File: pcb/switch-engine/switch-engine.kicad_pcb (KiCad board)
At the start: 10 copper layers, 135 x 111 mm, 369 parts, among them J1 CONN_PCIE_PWR_8PIN, J10 CORTEX_DEBUG_ETM, J11 SMPM, J12 CONN_01X03, J13 PMOD_HOST, J14 ARF6-08-S-D-A-K-TR, J15 ARF6-08-S-D-A-K-TR, J16 CONN_01X10, J17 ARF6-08-S-D-A-K-TR, J18 ARF6-08-S-D-A-K-TR, J19 CONN_01X10, J2 CONN_IBC_MGMT, J20 0826-1G1T-23-F, J21 ARF6-08-S-D-A-K-TR, J22 ARF6-08-S-D-A-K-TR, J23 CONN_01X10, J24 SMPM, J26 RJ45, J3 CONN_01X03, J4 CORTEX_DEBUG_ETM, J5 FAN_01, J6 FAN_01, J7 JUMPER_0402, J8 XILINX_JTAG, J9 PMOD_HOST, M1 SCREWHOLE, M2 SCREWHOLE, M3 SCREWHOLE, M4 SCREWHOLE, M5 LOGO, M6 LOGO, M7 LOGO, M8 960-27-23-D-AB-0, M9 FAN, Q2 SSM6N58NU, SW1 SWITCH, SW2 SWITCH, U1 STM32L431-QFN48, U10 74LVC1T45, U11 74LVC1T45, U12 74LVC1T45, U13 MT25QU256ABA8E12-0AUT, U14 ECS-1612MV-250-CN, U15 SIT9121AI-2BF-XXS156.250000G, U17 AT24MAC402, U18 74LVC1T45, U19 74LVC1T45, U2 MYMGK1R812ERSR, U20 74LVC1T45, U21 74LVC1T45, U22 ECS-1612MV-250-CN, U23 KSZ9031RN, U24 ESD224DQAR, U25 SIT9121AI-2BF-XXS156.250000G, U26 ESD224DQAR, U27 SIT9121AI-2BF-XXS156.250000G, U28 ADP1740ACPZ-2.5-R7, U29 ADM3101E_QFN, U3 MYMGK1R812ERSR, U4 MYMGK00506ERSR, U5 MYMGK00504ERSR, U6 MYMGK00504ERSR, U7 ADP1740ACPZ-1.8-R7, U8 XCKU5P-2FFVB676I, U9 STM32H735-UFBGA176-25

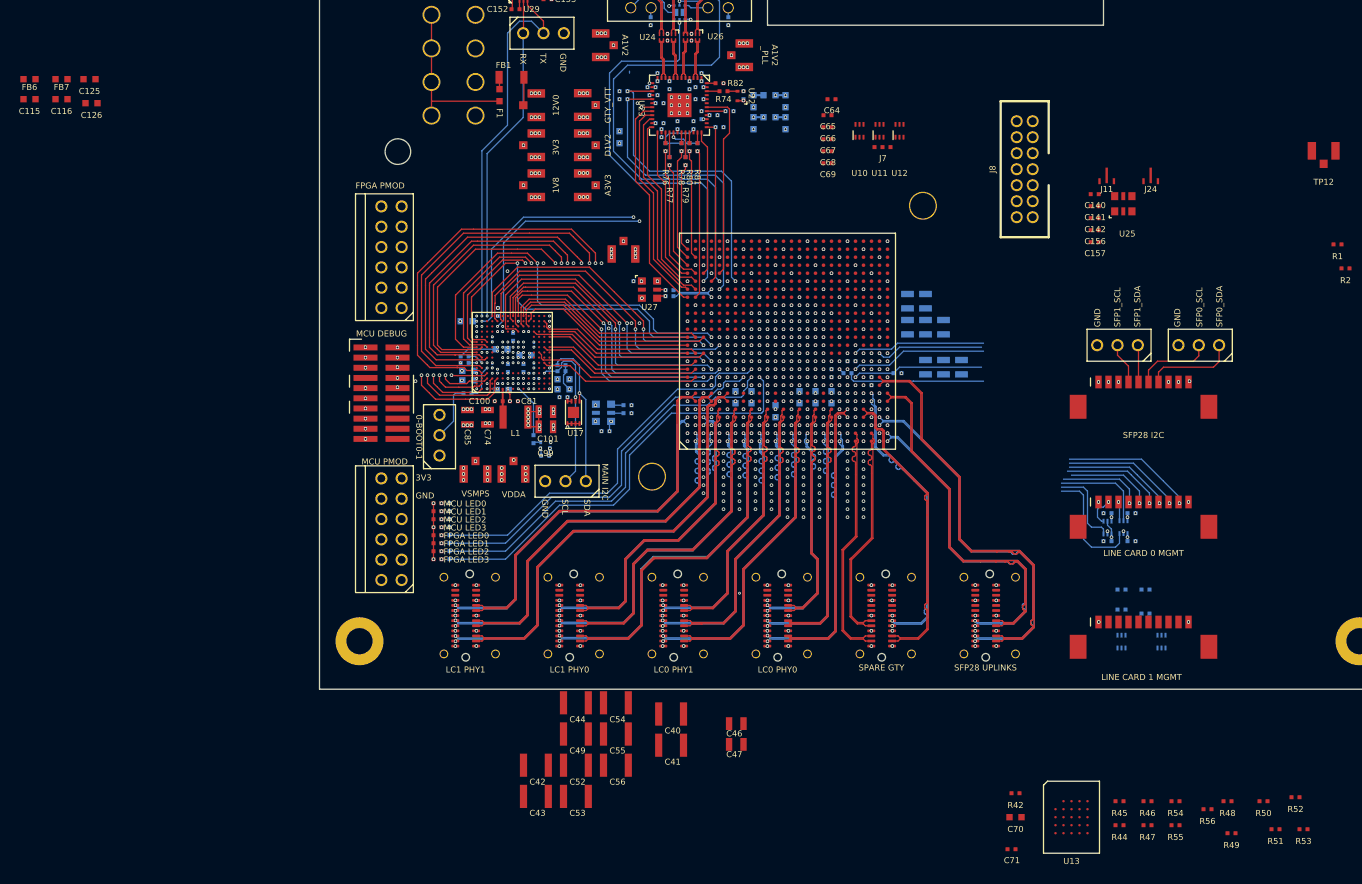
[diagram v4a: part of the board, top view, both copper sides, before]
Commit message: Continued routing main MCU and FPGA support parts, hooked up part of boot flash
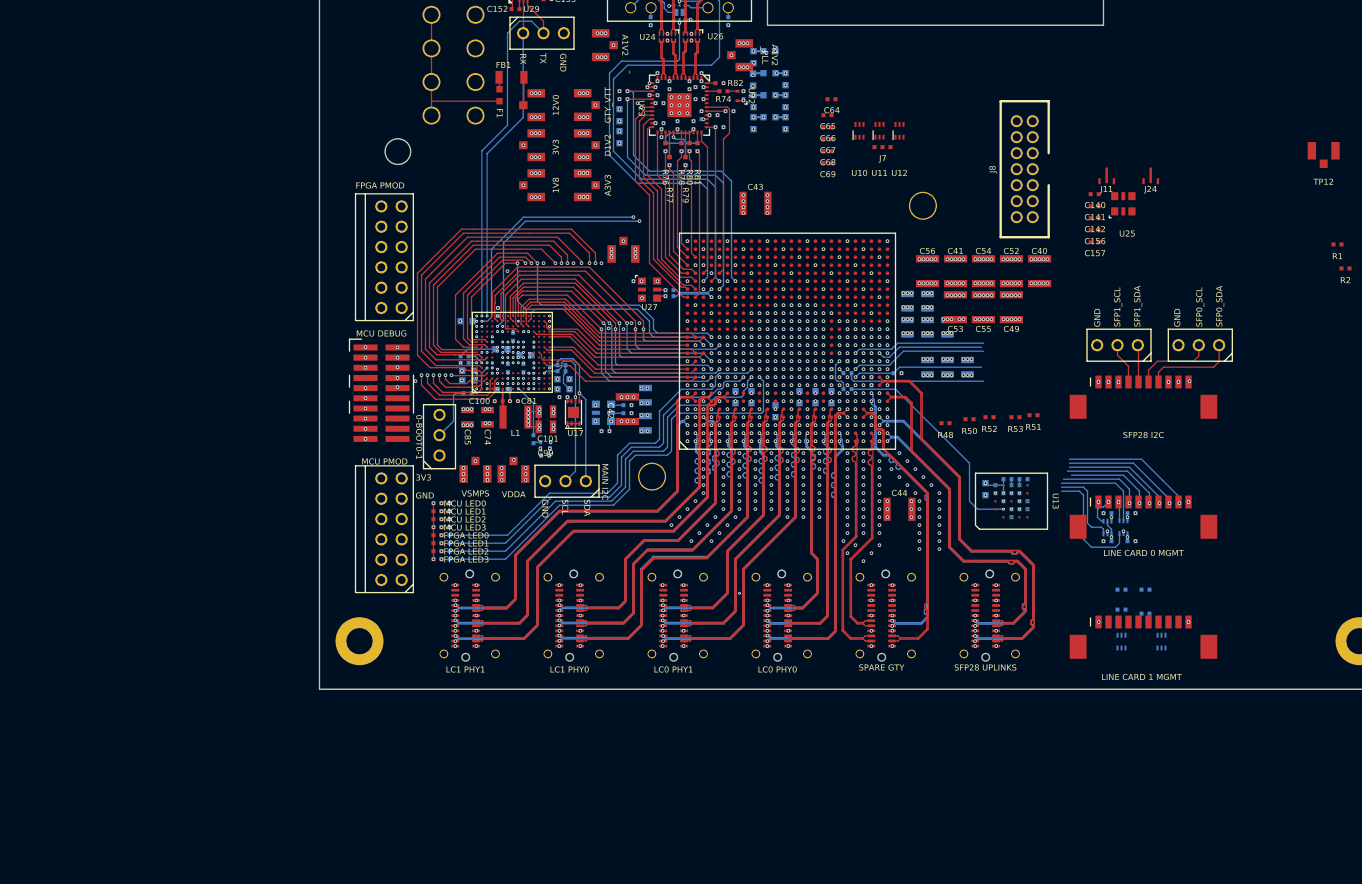
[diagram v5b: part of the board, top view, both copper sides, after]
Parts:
- C115, C116, C125, C126, C46, C47, C70, C71, FB6, FB7, R42, R44, R45, R46, R47, R49, R54, R55, R56: moved to B.Cu
- moved C115 94.5 mm to (95.2, 65.8), turned to -90 degrees
- moved FB6 92.5 mm to (93.2, 65.0), turned to 180 degrees
- moved FB7 88.6 mm to (93.2, 62.2), turned to 180 degrees
- moved C125 83.0 mm to (91.2, 65.8), turned to -90 degrees
- moved C126 82.9 mm to (91.2, 63.0), turned to -90 degrees
- moved C52 82.3 mm to (123.5, 89.8), turned to 90 degrees
- moved C43 79.1 mm to (91.5, 81.2)
- moved C53 77.4 mm to (116.5, 94.2), turned to -90 degrees
- moved C49 76.2 mm to (123.5, 94.2), turned to -90 degrees
- moved R49 73.4 mm to (103.0, 104.5)
- moved C56 73.0 mm to (113.0, 89.8), turned to 90 degrees
- moved C40 72.0 mm to (127.0, 89.8), turned to 90 degrees
- moved C54 70.9 mm to (120.0, 89.8), turned to 90 degrees
- moved C55 70.4 mm to (120.0, 94.2), turned to -90 degrees
- moved C116 69.8 mm to (74.5, 70.2), turned to -90 degrees
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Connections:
- net Net-(J7-P2) renamed /FPGA support/POR_OVERRIDE
- U8 pad AD15: unconnected-(U8J-IO_L3P_AD9P_84-PadAD15) -> /Line card interfaces/LC1_I2C_SCL
- U8 pad AE13: unconnected-(U8J-IO_L2P_AD10P_84-PadAE13) -> /Line card interfaces/LC0_SPI_MOSI
- U8 pad AE15: unconnected-(U8J-IO_L3N_AD9N_84-PadAE15) -> /Line card interfaces/LC0_SPI_MISO
- U8 pad AF13: unconnected-(U8J-IO_L2N_AD10N_84-PadAF13) -> /Line card interfaces/LC1_SPI_MOSI
- U8 pad AF14: unconnected-(U8J-IO_L1P_AD11P_84-PadAF14) -> /Line card interfaces/LC0_I2C_SDA
- U8 pad AF15: unconnected-(U8J-IO_L1N_AD11N_84-PadAF15) -> /Line card interfaces/LC0_I2C_SCL
- U8 pad W12: /Line card interfaces/LC0_I2C_SDA -> unconnected-(U8J-IO_L12P_AD0P_84-PadW12)
- U8 pad W13: /Line card interfaces/LC0_I2C_SCL -> unconnected-(U8J-IO_L12N_AD0N_84-PadW13)
- U8 pad W14: /Line card interfaces/LC0_SPI_MOSI -> unconnected-(U8J-IO_L10P_AD2P_84-PadW14)
- U8 pad W15: /Line card interfaces/LC0_SPI_MISO -> unconnected-(U8J-IO_L10N_AD2N_84-PadW15)
- U8 pad W16: /Line card interfaces/LC1_I2C_SDA -> unconnected-(U8J-IO_L9P_AD3P_84-PadW16)
- U8 pad Y15: /Line card interfaces/LC1_SPI_MOSI -> unconnected-(U8J-IO_L7P_HDGC_AD5P_84-PadY15)
- U8 pad Y16: /Line card interfaces/LC1_I2C_SCL -> /Line card interfaces/LC1_I2C_SDA
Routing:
- net /GND: track 1472.5 -> 1635.8 mm, vias 575 -> 712
- net /1V8: track 170.9 -> 262.4 mm, vias 32 -> 54
- net /FPGA support/FPGA_FLASH_SCK: track 0.00 -> 28.0 mm, vias 0 -> 1
- net /FPGA support/VCCINT: track 67.6 -> 92.7 mm, vias 40 -> 86
- net /3V3: track 459.5 -> 474.7 mm, vias 53 -> 65
- net /FPGA support/POR_OVERRIDE: track 0.00 -> 15.2 mm, vias 0 -> 1
- net /RGMII PHY/A1V2: track 14.1 -> 27.8 mm, vias 3 -> 4
- net /GTY_VTT: track 118.2 -> 126.2 mm, vias 18 -> 21
- net /RGMII PHY/A1V2_PLL: track 7.96 -> 15.1 mm, vias 2 -> 4
- net Net-(U8A-CCLK_0): track 0.00 -> 4.41 mm
- net /MCU/FPGA_LED_3: track 54.0 -> 55.9 mm
- net /MCU/FPGA_LED_2: track 50.0 -> 51.7 mm
- net /MCU/FPGA_LED_0: track 49.5 -> 51.1 mm
- net /MCU/FPGA_LED_1: track 48.1 -> 49.7 mm
- net /RGMII PHY/D1V2: track 33.8 -> 35.0 mm, vias 8 -> 9
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
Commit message: Routing cleanup around FMC, still needs a lot more
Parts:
- moved TP7 207.1 mm to (71.5, 124.5)
- moved TP29 113.3 mm to (177.0, 122.0)
- moved C146 103.4 mm to (182.0, 146.5)
- moved C147 103.4 mm to (178.5, 146.5)
- moved C148 103.4 mm to (192.5, 144.0)
- moved C35 103.4 mm to (182.0, 134.5)
- moved C36 103.4 mm to (178.5, 134.5)
- moved C37 103.4 mm to (193.8, 133.5)
- moved TP11 103.4 mm to (198.5, 132.5)
- moved TP24 103.4 mm to (199.0, 143.0)
- moved U28 103.4 mm to (188.0, 144.5)
- moved U7 103.4 mm to (187.5, 134.0)
- moved M5 94.6 mm to (179.5, 101.0)
- moved M6 94.6 mm to (177.0, 107.5)
- moved M7 94.6 mm to (176.0, 114.4)
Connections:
- U8 pad F10: /MCU/FMC_A23 -> /MCU/FMC_NBL1
- U8 pad G10: /MCU/FMC_NBL1 -> /MCU/FMC_A23
- U9 pad A2: /MCU/SFP0_SCL -> unconnected-(U9B-PB8-PadA2)
- U9 pad B3: /MCU/SFP0_SDA -> unconnected-(U9B-PB9-PadB3)
- U9 pad M13: unconnected-(U9H-PH11-PadM13) -> /MCU/SFP0_SCL
- U9 pad M14: unconnected-(U9H-PH9-PadM14) -> /Power Supply/FAN2_TACH
- U9 pad N11: unconnected-(U9F-PF13-PadN11) -> /Power Supply/FAN2_PWM
- U9 pad N15: unconnected-(U9H-PH12-PadN15) -> /MCU/SFP0_SDA
- U9 pad N5: /Power Supply/FAN2_PWM -> unconnected-(U9A-PA3-PadN5)
- U9 pad P1: /Power Supply/FAN1_TACH -> unconnected-(U9A-PA0-PadP1)
- U9 pad P11: unconnected-(U9F-PF12-PadP11) -> /Power Supply/FAN1_PWM
- U9 pad P15: unconnected-(U9H-PH6-PadP15) -> /Power Supply/FAN1_TACH
- U9 pad P2: /Power Supply/FAN2_TACH -> unconnected-(U9A-PA1-PadP2)
- U9 pad R2: /Power Supply/FAN1_PWM -> unconnected-(U9A-PA2-PadR2)
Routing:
- net /MCU/FMC_NBL1: track 62.8 -> 31.2 mm
- net /MCU/FMC_A23: track 64.4 -> 33.6 mm
- net /MCU/FMC_NBL0: track 70.6 -> 64.4 mm
- net /MCU/FMC_NL_NADV: track 67.8 -> 61.8 mm
- net /MCU/FMC_A24: track 65.0 -> 59.2 mm
- net /MCU/FMC_NE2: track 63.6 -> 58.1 mm
- net /MCU/FMC_A25: track 67.8 -> 62.6 mm
- net /MCU/FMC_NWE: track 61.5 -> 56.4 mm
- net /GND: track 1635.8 -> 1639.5 mm, vias 712 -> 713
- net /MCU/FMC_AD2: track 46.9 -> 44.5 mm
- net /MCU/VSMPS: track 46.4 -> 48.8 mm
- net /MCU/FPGA_PMOD_DQ6: track 52.8 -> 54.9 mm
- net /MCU/FPGA_PMOD_DQ2: track 50.4 -> 51.8 mm
- net /MCU/FMC_CLK: track 50.6 -> 49.3 mm
- net /MCU/FPGA_PMOD_DQ7: track 56.8 -> 57.6 mm
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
